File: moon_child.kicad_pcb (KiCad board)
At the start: 4 copper layers, 63.2 x 63.2 mm, 183 parts, among them J1 Motor0, J10 USB_C_Receptacle_USB2.0_14P, J2 Motor1, J3 Battery Input, J4 Micro_SD_Card_Det1, J5 Conn_01x04, J6 Conn_01x04, J7 Conn_02x05_Odd_Even, J8 Conn_01x03, J9 debug_probe, Q1 BSP613P, Q2 Q_NPN_BCE, SW1 SW_Omron_B3FS, U1 DRV8871DDA, U2 DRV8871DDA, U3 AP62250Z6, U4 IIM-42652, U5 BME280, U6 RP2350B-QFN80, U7 INA180A1, U8 16Mbit PSRAM, U9 16Mbit PSRAM, X1 ASE-12.000MHZ-L-C-T

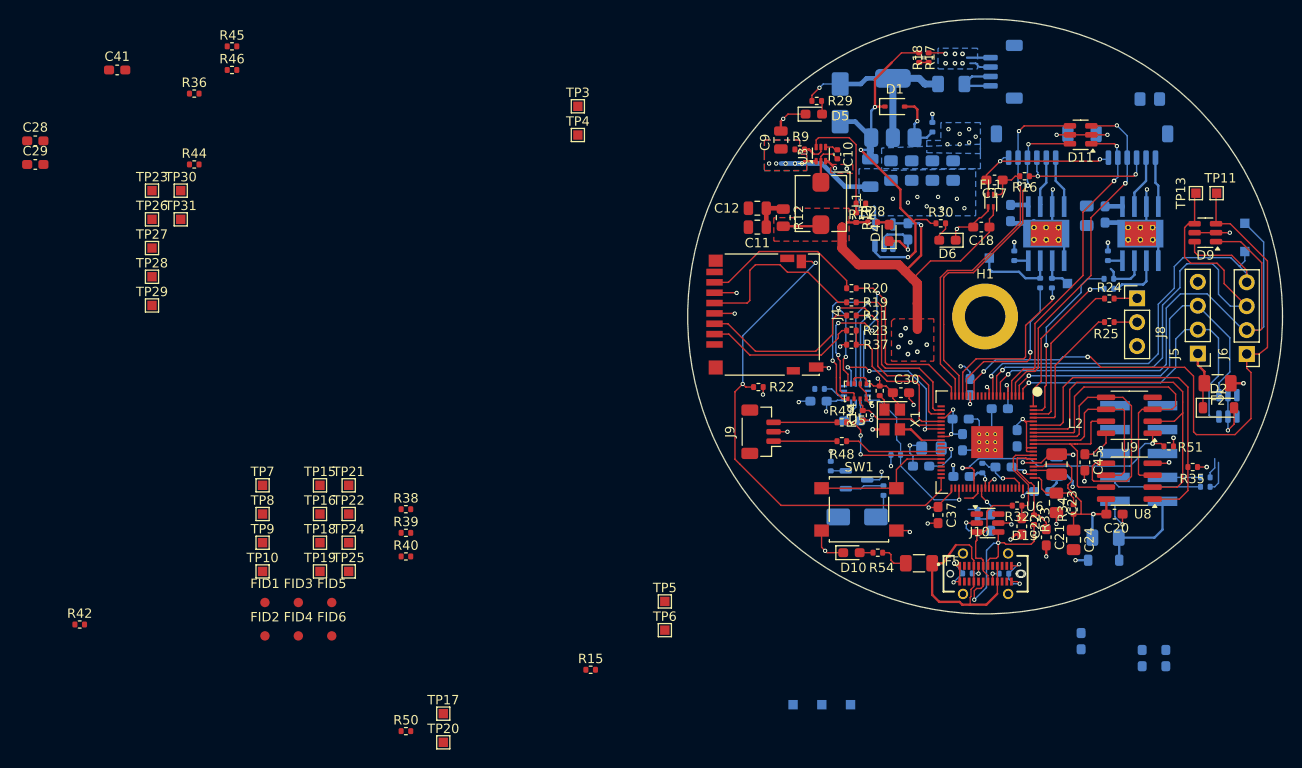
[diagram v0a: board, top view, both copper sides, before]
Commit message: Layout updates
testpoints, usb power, etc.
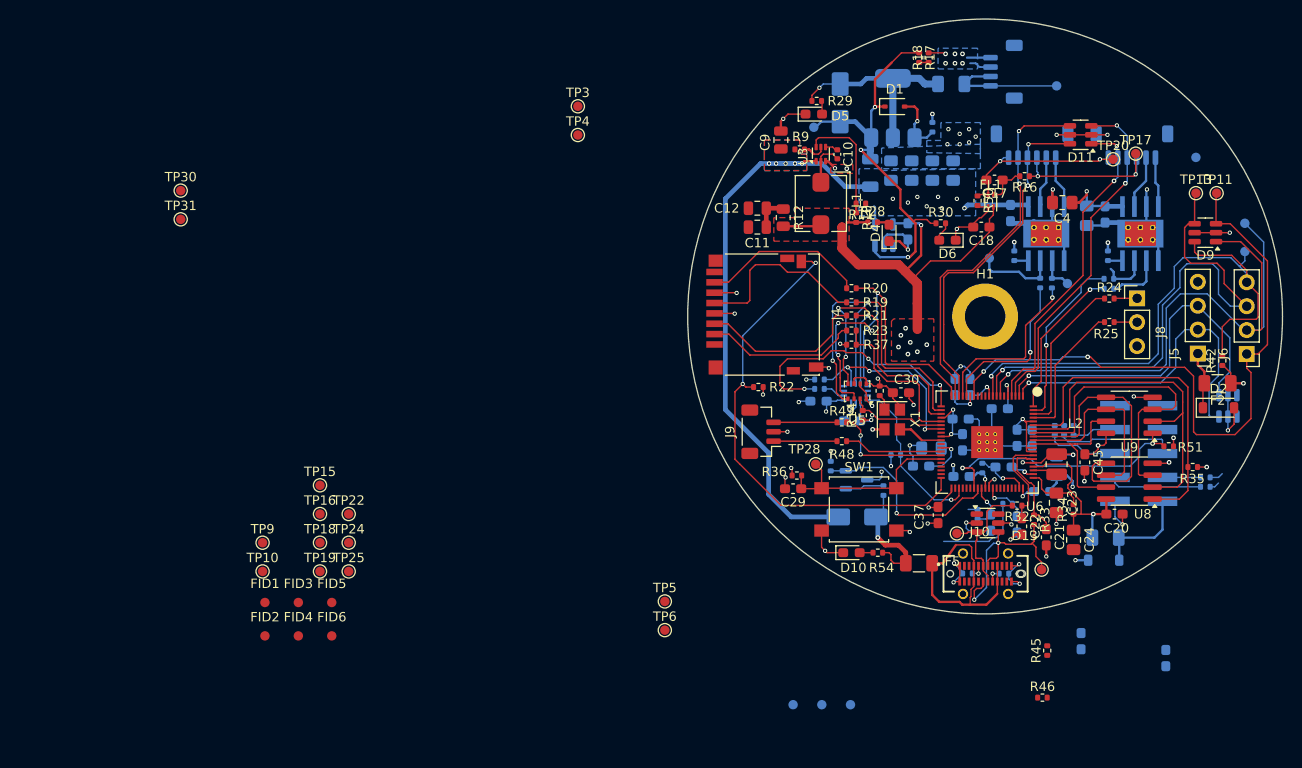
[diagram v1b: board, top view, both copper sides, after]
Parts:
- removed TP27: 1V1, TestPoint:TestPoint_Pad_1.0x1.0mm
- removed TP29: Xin, TestPoint:TestPoint_Pad_1.0x1.0mm
- C28, C41, R15, R38, R39, R40, R44: moved to B.Cu
- C4: moved to F.Cu
- TP1, TP10, TP11, TP12, TP13, TP14, TP15, TP16, TP17, TP18, TP19, TP2, TP20, TP22, TP23, TP24, TP25, TP26, TP28, TP3, TP30, TP31, TP32, TP33, TP34, TP4, TP5, TP6, TP9: footprint TestPoint:TestPoint_Pad_1.0x1.0mm -> TestPoint:TestPoint_Pad_D1.0mm
- TP21, TP8: footprint TestPoint:TestPoint_Pad_1.0x1.0mm -> TestPoint:TestPoint_Pad_D1.0mm; moved to B.Cu
- TP7: value TestPoint -> Input_V; footprint TestPoint:TestPoint_Pad_1.0x1.0mm -> TestPoint:TestPoint_Pad_D1.0mm; moved to B.Cu
- moved R42 124.6 mm to (184.4, 93.2), turned to 90 degrees
- moved R46 108.9 mm to (165.3, 129.0)
- moved R45 107.8 mm to (165.8, 124.0), turned to 90 degrees
- moved C41 104.8 mm to (164.2, 101.4), turned to -90 degrees
- moved C28 102.7 mm to (157.6, 96.0), turned to 90 degrees
- moved TP26 101.6 mm to (165.2, 115.4)
- moved TP21 96.5 mm to (181.6, 71.6), turned to 180 degrees
- moved TP17 94.6 mm to (175.2, 71.2)
- moved TP7 94.4 mm to (166.8, 64.0), turned to 180 degrees
- moved TP20 94.4 mm to (172.8, 71.8)
- moved R44 93.6 mm to (161.6, 108.4), turned to 180 degrees
- moved TP23 93.0 mm to (156.2, 111.5)
- moved C29 87.6 mm to (138.8, 106.8), turned to 180 degrees
- moved R50 82.9 mm to (158.4, 76.2), turned to -90 degrees
- moved R36 75.8 mm to (139.2, 105.4)
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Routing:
- net Board_VBATT: track 17.9 -> 79.7 mm, vias 13 -> 14
- net /raspi/IMU_CLK: track 0.00 -> 27.4 mm, vias 0 -> 3
- net /raspi/~{USB_V_present}: track 4.05 -> 21.7 mm, vias 0 -> 1
- net GND: track 146.5 -> 161.1 mm, vias 57 -> 59
- net /raspi/Spare_CS_1: track 0.00 -> 12.5 mm
- net /connectors+mechanical/GPS_INT: track 51.2 -> 62.8 mm
- net /connectors+mechanical/VBATT_I: track 0.00 -> 9.65 mm
- net /raspi/Spare_CS_2: track 0.00 -> 7.61 mm
- net 3v3: track 122.7 -> 130.0 mm, vias 29 -> 31
- net USB_VBUS: track 5.90 -> 13.0 mm, vias 0 -> 1
- net /connectors+mechanical/Input_Voltage: track 5.96 -> 13.0 mm
- net /raspi/~{RESET}: track 15.1 -> 21.6 mm
- net Net-(U6-GPIO41_ADC1): track 0.00 -> 4.82 mm, vias 0 -> 1
- net /raspi/Spare_CS_0: track 0.00 -> 4.64 mm
- net /connectors+mechanical/DP-: track 20.2 -> 23.4 mm
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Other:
- board text added: "Input_V"

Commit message: layout updates
removes ADC 2 and ADC 3 connections for space reasons
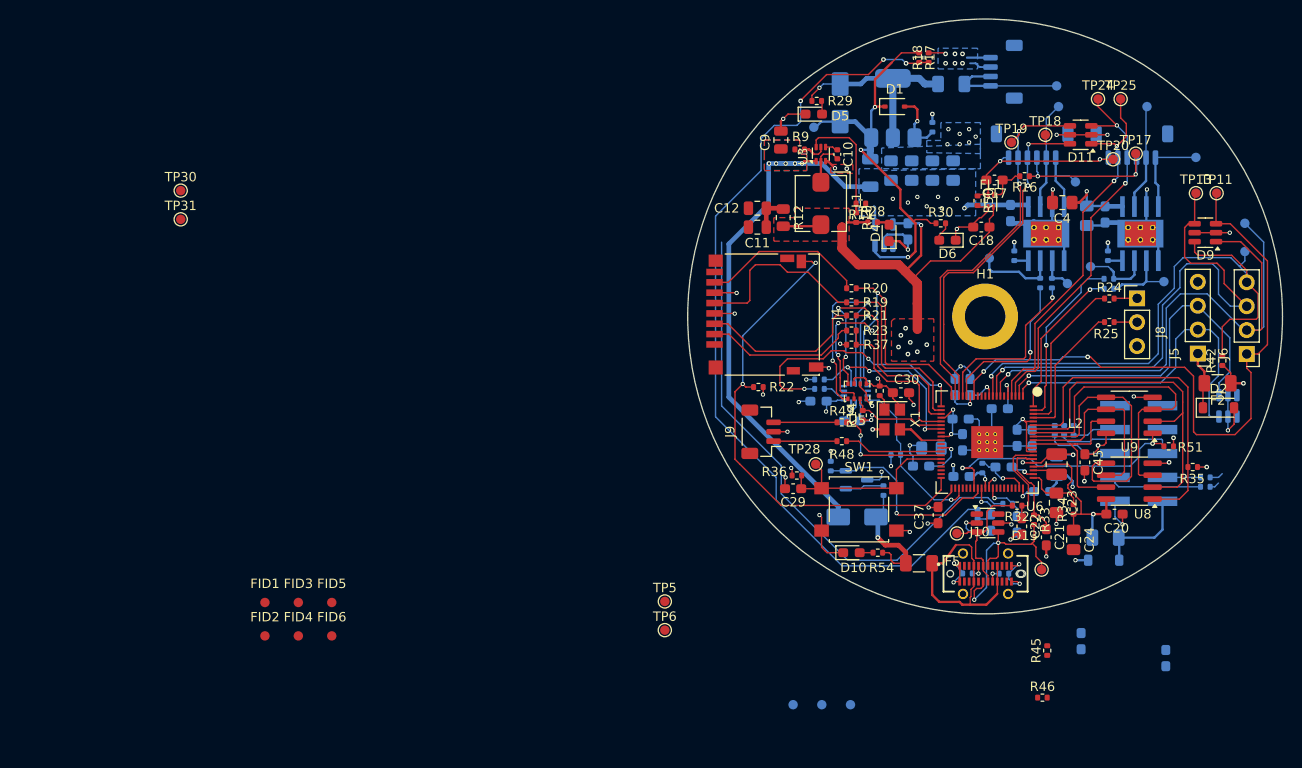
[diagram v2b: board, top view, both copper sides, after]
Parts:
- removed TP10: GPS_TX, TestPoint:TestPoint_Pad_D1.0mm
- removed TP9: GPS_RX, TestPoint:TestPoint_Pad_D1.0mm
- TP15, TP16, TP22, TP3, TP4: moved to B.Cu
- moved TP25 96.2 mm to (173.6, 65.4)
- moved TP22 95.2 mm to (176.4, 66.2), turned to 180 degrees
- moved TP24 92.5 mm to (171.2, 65.4)
- moved TP16 89.6 mm to (167.0, 66.2), turned to 180 degrees
- moved TP18 88.4 mm to (165.6, 69.2)
- moved TP15 86.5 mm to (168.8, 74.2), turned to 180 degrees
- moved TP19 86.5 mm to (162.0, 70.0)
- moved TP4 64.2 mm to (178.2, 84.8), turned to 180 degrees
- moved TP3 57.1 mm to (170.4, 83.2), turned to 180 degrees
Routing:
- net /connectors+mechanical/VBATT_Sense: track 2.00 -> 92.7 mm, vias 0 -> 3
- net /connectors+mechanical/VBATT_I: track 9.65 -> 58.9 mm
- net Motor0_-: track 5.80 -> 11.8 mm
- net /connectors+mechanical/Encoder1_B: track 34.7 -> 40.4 mm
- net Motor1_-: track 5.86 -> 11.5 mm
- net Motor1_+: track 5.48 -> 9.79 mm
- net Board_VBATT: track 79.7 -> 75.9 mm
- net /connectors+mechanical/Encoder1_A: track 37.4 -> 41.0 mm
- net Motor0_+: track 5.60 -> 7.95 mm
- net Net-(U2-IN1): track 5.07 -> 7.32 mm
- net Net-(U2-IN2): track 5.98 -> 7.86 mm
- net GND: track 161.1 -> 162.9 mm
- net /connectors+mechanical/Encoder0_B: track 39.7 -> 41.2 mm
- net /connectors+mechanical/Encoder0_A: track 37.2 -> 38.1 mm

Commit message: layout updates
SPI routes
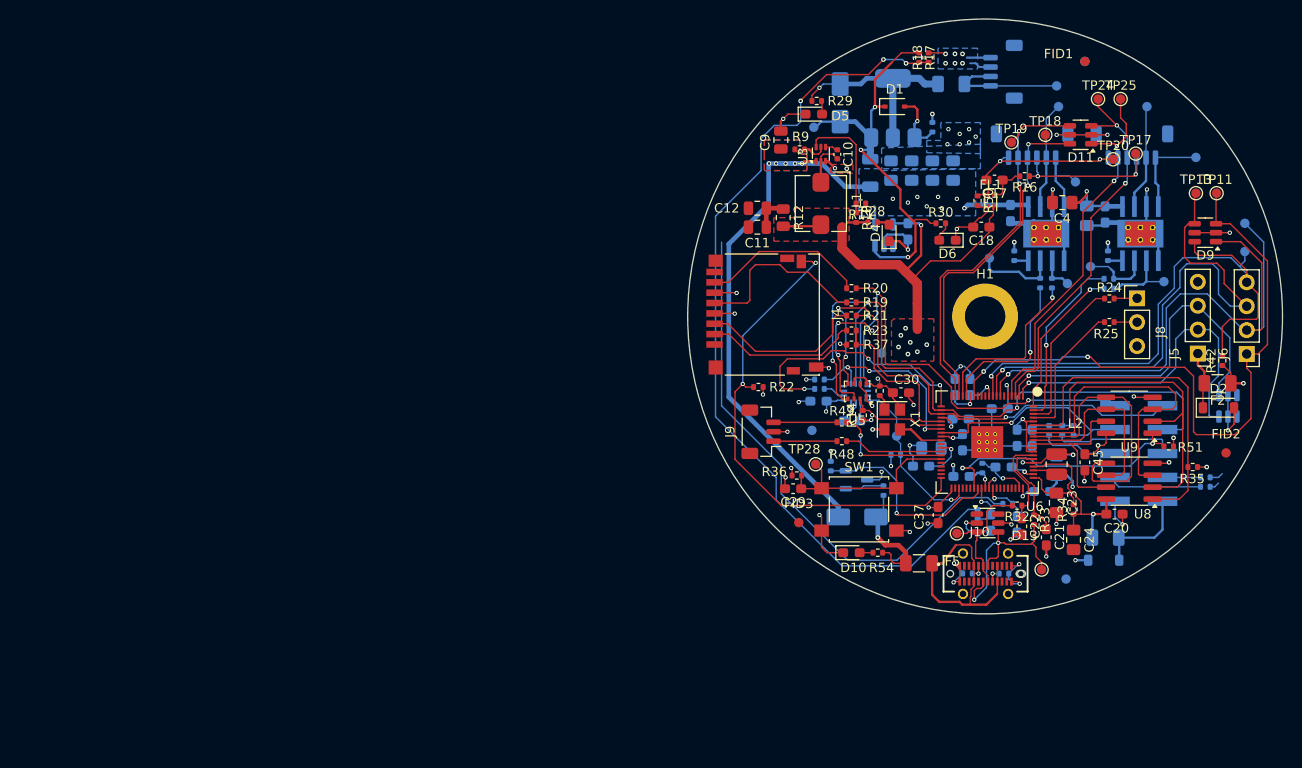
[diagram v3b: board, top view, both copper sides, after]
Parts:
- removed C33, C34: 1.6nF, Capacitor_SMD:C_0603_1608Metric_Pad1.08x0.95mm_HandSolder
- removed R45, R46: 10K, Resistor_SMD:R_0402_1005Metric
- removed TP30: ADC_2, TestPoint:TestPoint_Pad_D1.0mm
- removed TP31: ADC_3, TestPoint:TestPoint_Pad_D1.0mm
- removed TP32, TP33, TP34: Spare, TestPoint:TestPoint_Pad_D1.0mm
- FID4, FID5, FID6, TP5, TP6: moved to B.Cu
- moved FID1 104.4 mm to (169.8, 61.4)
- moved FID2 104.0 mm to (184.8, 103.0)
- moved FID4 103.5 mm to (169.8, 61.4), turned to 180 degrees
- moved FID6 78.3 mm to (167.8, 116.4), turned to 180 degrees
- moved FID5 54.2 mm to (140.8, 100.6), turned to 180 degrees
- moved FID3 53.8 mm to (139.4, 110.4)
- moved TP6 37.4 mm to (148.2, 92.4), turned to 180 degrees
- moved TP5 30.3 mm to (149.8, 101.2), turned to 180 degrees
- moved R40 0.60 mm to (166.0, 100.6)
- moved R38 0.20 mm to (167.4, 100.6)
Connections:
- U6 pad 11: Net-(U6-GPIO12) -> unconnected-(U6-GPIO12-Pad11)
- U6 pad 12: Net-(U6-GPIO13) -> unconnected-(U6-GPIO13-Pad12)
- U6 pad 13: Net-(U6-GPIO14) -> unconnected-(U6-GPIO14-Pad13)
- U6 pad 53: Net-(U6-GPIO42_ADC2) -> unconnected-(U6-GPIO42_ADC2-Pad53)
- U6 pad 54: Net-(U6-GPIO43_ADC3) -> unconnected-(U6-GPIO43_ADC3-Pad54)
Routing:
- net /sensors/MCU_SCLK: track 43.1 -> 76.5 mm, vias 2 -> 3
- net /sensors/MCU_SDO: track 37.8 -> 63.0 mm, vias 3 -> 4
- net /sensors/MCU_SDI: track 44.1 -> 63.0 mm, vias 4 -> 5
- net /raspi/Spare_CS_0: track 4.64 -> 23.2 mm, vias 0 -> 1
- net 3v3: track 130.0 -> 133.1 mm
- net /raspi/IMU_CLK: track 27.4 -> 28.6 mm
- net /raspi/Spare_CS_2: track 7.61 -> 8.21 mm

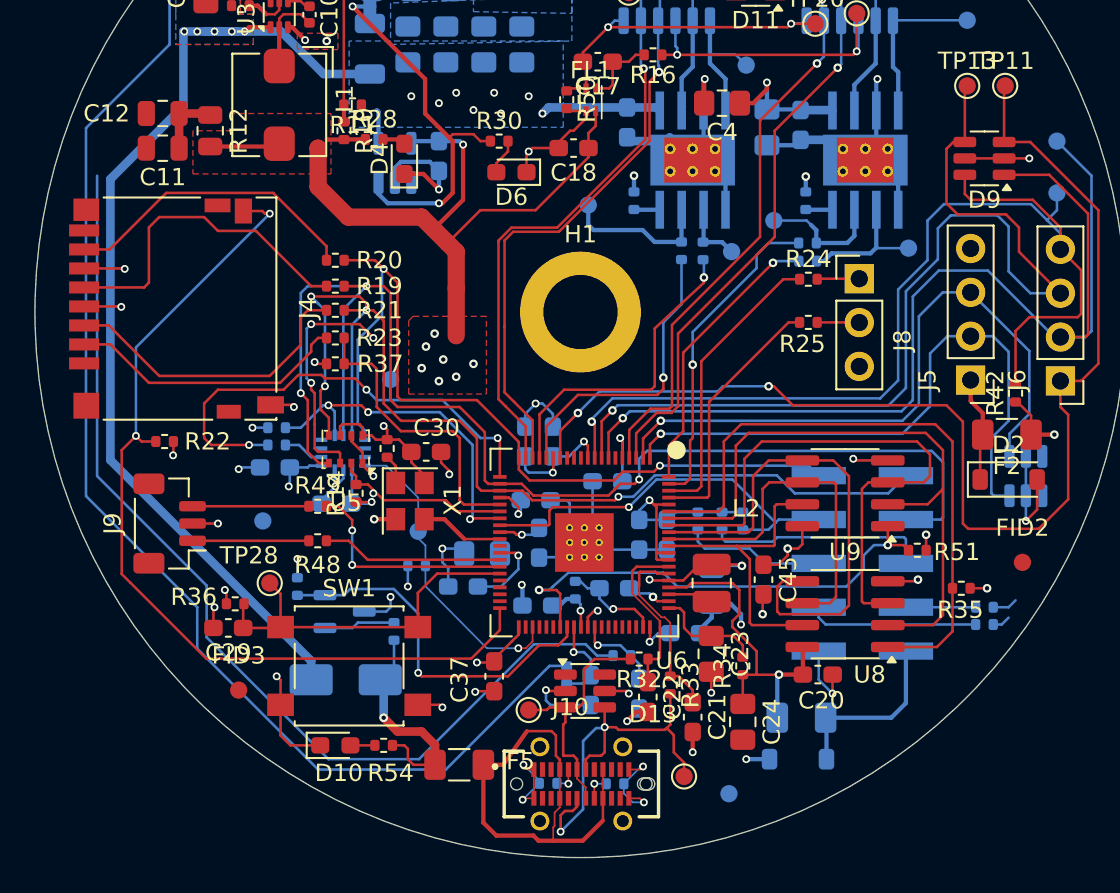
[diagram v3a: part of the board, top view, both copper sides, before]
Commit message: Routing updates
All nets connected, still need to clear DRCS and fix silks
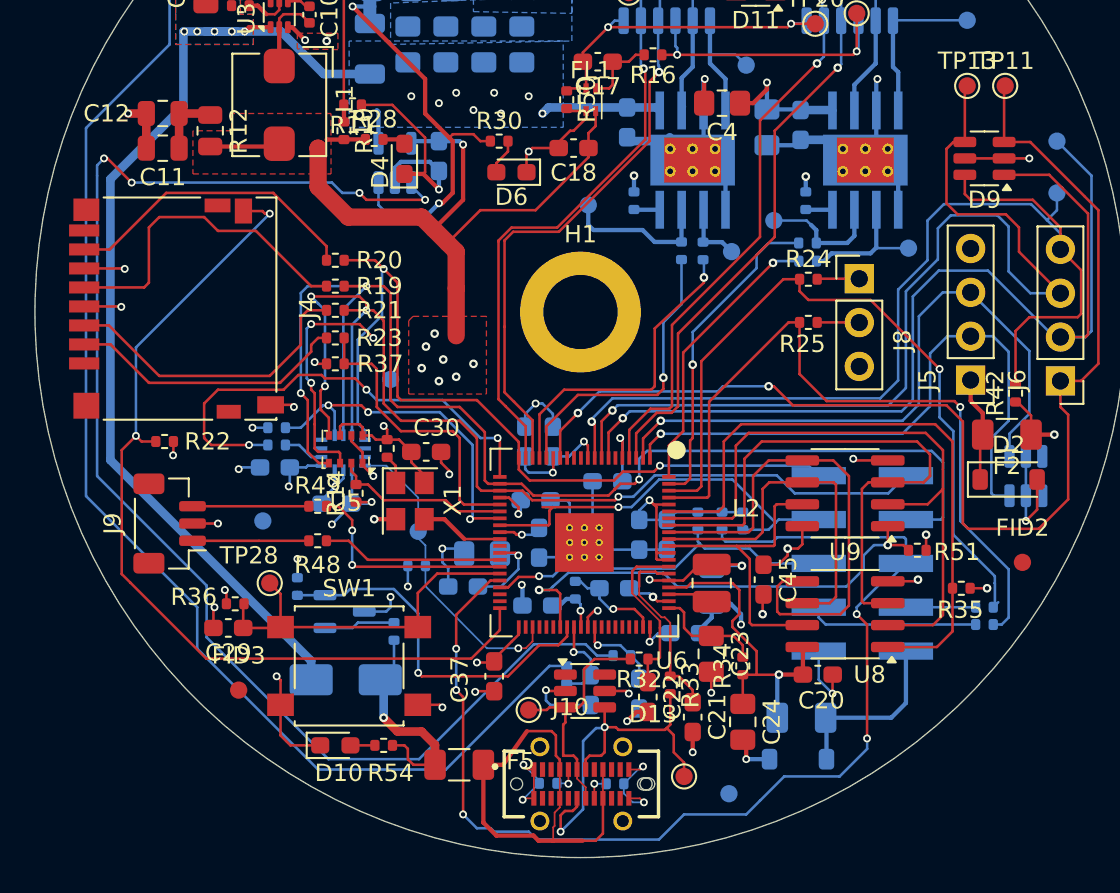
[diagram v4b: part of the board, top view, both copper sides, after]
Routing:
- net /raspi/Spare_CS_1: track 12.8 -> 66.4 mm, vias 0 -> 5
- net /raspi/Raspi_TX: track 16.0 -> 42.5 mm, vias 0 -> 1
- net /raspi/Raspi_RX: track 18.3 -> 43.1 mm, vias 0 -> 1
- net /connectors+mechanical/VBATT_I: track 58.9 -> 81.0 mm, vias 0 -> 4
- net /raspi/Spare_CS_2: track 8.21 -> 20.8 mm, vias 0 -> 1
- net GND: track 162.9 -> 173.8 mm, vias 59 -> 60
- net /raspi/1V1: track 16.9 -> 23.9 mm
- net 3v3: track 133.1 -> 134.8 mm, vias 31 -> 32
- net Net-(D1-K): track 44.9 -> 46.0 mm
- net /raspi/Spare_CS_0: track 23.2 -> 23.8 mm
- net /raspi/BAR_CS: track 10.6 -> 10.5 mm, vias 1 -> 0

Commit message: silkscreen cleanup
Cleaned up silks
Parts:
- moved TP4 0.20 mm to (178.2, 85.0)
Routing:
- net /raspi/Spare_CS_0: track 23.8 -> 23.2 mm

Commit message: silk fixes
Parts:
- moved R9 0.53 mm to (139.2, 70.3), turned to 90 degrees
- moved C12 0.28 mm to (134.8, 76.8)
- moved C11 0.20 mm to (134.8, 79.0)
- moved R18 0.20 mm to (153.4, 61.0)
- moved R28 0.05 mm to (147.2, 78.5)
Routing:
- net Net-(U3-EN): track 2.55 -> 3.75 mm

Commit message: CBjamo updats
Added J11 to accommodate batteries on both sides and changed pinout of J8 to have ground in the middle.
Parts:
- added J11: Battery Input, Connector_JST:JST_SH_BM04B-SRSS-TB_1x04-1MP_P1.00mm_Vertical, F.Cu at (161.1, 62.5)
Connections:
- J8 pad 2: /raspi/Debug_TX -> GND
- J8 pad 3: GND -> /raspi/Debug_TX
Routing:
- net GND: track 173.8 -> 180.1 mm
- net /connectors+mechanical/Input_Voltage: vias 0 -> 5
- added copper zone on B.Cu, net /connectors+mechanical/Input_Voltage
- added copper zone on F.Cu, net /connectors+mechanical/Input_Voltage

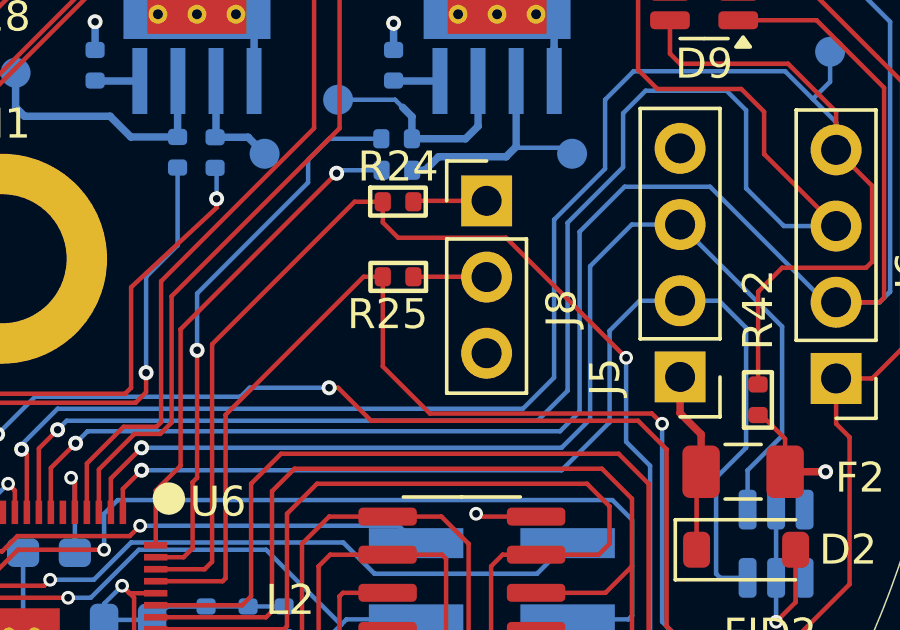
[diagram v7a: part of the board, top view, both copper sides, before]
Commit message: swapped J8 pinout
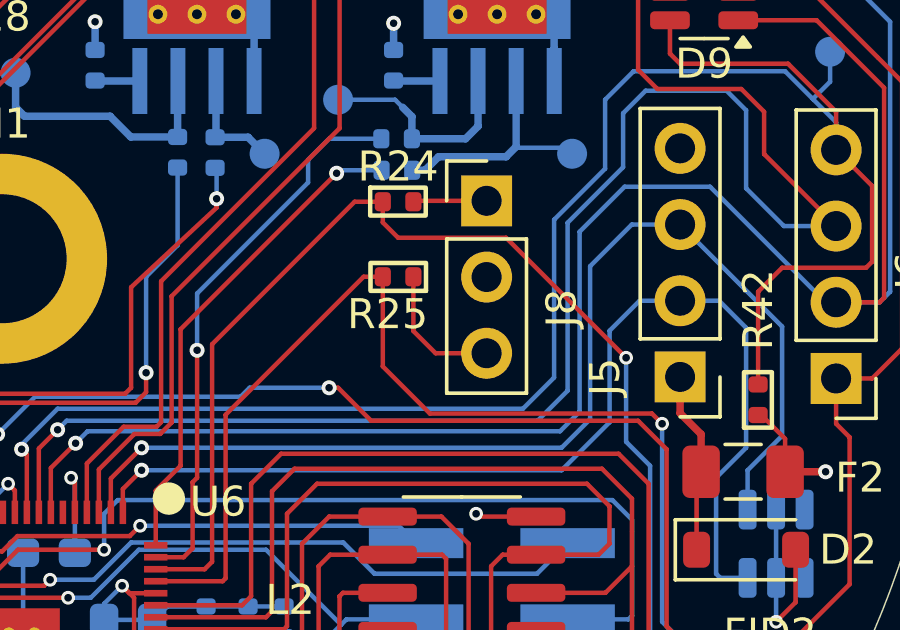
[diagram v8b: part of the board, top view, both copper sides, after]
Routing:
- net /raspi/Debug_TX: track 2.44 -> 4.56 mm
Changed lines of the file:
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@@
 	)
 	(segment
+		(start 175.34 89.1)
+		(end 175.35 89.11)
+		(width 0.15)
+		(layer "F.Cu")
+		(net 1)
+	)
+	(segment
 		(start 144.125 113.6)
 		(end 142.4 113.6)
@@
 	(segment
 		(start 172.91 89.1)
-		(end 175.34 89.1)
+		(end 172.91 90.91)
 		(width 0.15)
 		(layer "F.Cu")
@@
 	)
 	(segment
-		(start 175.34 89.1)
-		(end 175.35 89.11)
+		(start 173.65 91.65)
+		(end 175.35 91.65)
+		(width 0.15)
+		(layer "F.Cu")
+		(net 59)
+	)
+	(segment
+		(start 172.91 90.91)
+		(end 173.65 91.65)
 		(width 0.15)
 		(layer "F.Cu")
